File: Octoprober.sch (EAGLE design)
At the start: 101 parts, among them J1 10118193-0001LF, J2 26-60-4020, P1 TC33X-1, SW1 EVQ-Q2203W, SW2 EVQ-Q2203W, SW3 EVQ-Q2203W, SW4 EVQ-Q2203W, SW5 EVQ-Q2203W, U1 P8X32A-M44, U10 MAX31855KASA+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

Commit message: Finished preliminary routing
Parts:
- removed U18: AD7999YRJZ-1500RL7, PP_DigitalIC:AD799XSOT-23-8
- added TC1, TC2, TC3, TC4, TC5, TC6, TC7, TC8: (no value), PP_Connectors:PH_1X02HEADER_PTH
- SW1: value EVQ-Q2203W -> 101-0134-EV; device PP_Electromechanical:SPSTEVQ-Q2203W -> PP_Electromechanical:SPST101-0134-EV
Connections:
- net TP_T+_0: now also TC1.2
- net TP_T+_1: now also TC2.2
- net TP_T+_2: now also TC3.2
- net TP_T+_3: now also TC4.2
- net TP_T+_4: now also TC5.2
- net TP_T+_5: now also TC6.2
- net TP_T+_6: now also TC7.2
- net TP_T+_7: now also TC8.2
- net TP_T-_0: now also TC1.1
- net TP_T-_1: now also TC2.1
- net TP_T-_2: now also TC3.1
- net TP_T-_3: now also TC4.1
- net TP_T-_4: now also TC5.1
- net TP_T-_5: now also TC6.1
- net TP_T-_6: now also TC7.1
- net TP_T-_7: now also TC8.1
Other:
- moved on the sheet: C15, C16, C17, C18, C19, C20, C21, C22, U10, U7, U8, U9

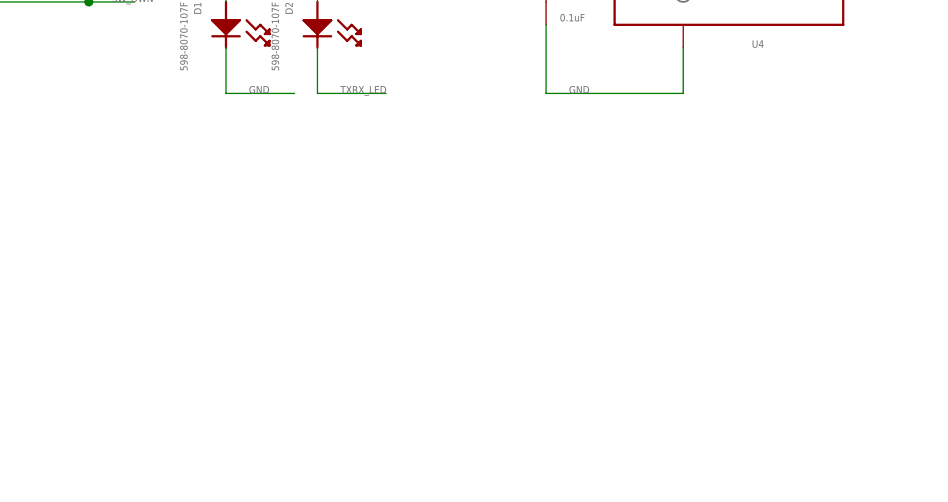
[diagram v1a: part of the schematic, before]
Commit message: Added RTC.
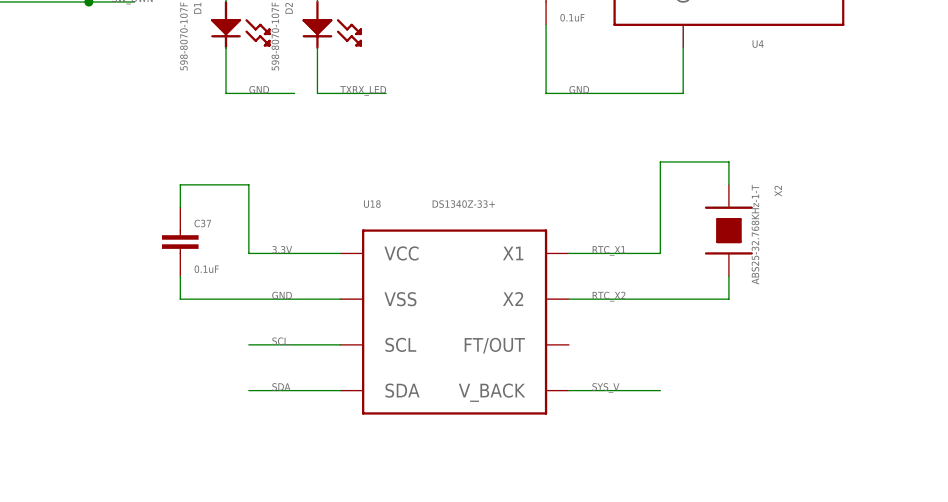
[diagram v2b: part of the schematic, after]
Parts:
- added C37: 0.1uF, PP_Passives:CAPACITOR_NON_POLAR0402
- added U18: DS1340Z-33+, PP_DigitalIC:DS1340SOIC-8
- added X2: ABS25-32.768KHz-1-T, PP_FreqCtrl:CRYSTAL8MM_X_3.8MM
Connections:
- new net RTC_X1: U18.X1, X2.P$1
- new net RTC_X2: U18.X2, X2.P$2
- net 3.3V: now also C37.1, U18.VCC
- net GND: now also C37.2, U18.VSS
- net SCL: now also U18.SCL
- net SDA: now also U18.SDA
- net SYS_V: now also U18.V_BACK
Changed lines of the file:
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@@
 <?xml version="1.0" encoding="utf-8"?>
 <!DOCTYPE eagle SYSTEM "eagle.dtd">
-<eagle version="6.3">
+<eagle version="6.5.0">
 <drawing>
 <settings>
@@
 <grid distance="0.1" unitdist="inch" unit="inch" style="lines" multiple="1" display="no" altdistance="0.01" altunitdist="inch" altunit="inch"/>
 <layers>
-<layer number="1" name="Top" color="14" fill="1" visible="yes" active="no"/>
+<layer number="1" name="Top" color="14" fill="1" visible="no" active="no"/>
 <layer number="2" name="Route2" color="1" fill="3" visible="no" active="no"/>
 <layer number="3" name="Route3" color="4" fill="3" visible="no" active="no"/>
@@
 <layer number="14" name="Route14" color="1" fill="6" visible="no" active="no"/>
 <layer number="15" name="Route15" color="4" fill="6" visible="no" active="no"/>
-<layer number="16" name="Bottom" color="13" fill="1" visible="yes" active="no"/>
-<layer number="17" name="Pads" color="2" fill="1" visible="yes" active="no"/>
-<layer number="18" name="Vias" color="2" fill="1" visible="yes" active="no"/>
-<layer number="19" name="Unrouted" color="6" fill="1" visible="yes" active="no"/>
-<layer number="20" name="Dimension" color="15" fill="1" visible="yes" active="no"/>
-<layer number="21" name="tPlace" color="7" fill="1" visible="yes" active="no"/>
-<layer number="22" name="bPlace" color="7" fill="1" visible="yes" active="no"/>
-<layer number="23" name="tOrigins" color="15" fill="1" visible="yes" active="no"/>
-<layer number="24" name="bOrigins" color="15" fill="1" visible="yes" active="no"/>
-<layer number="25" name="tNames" color="7" fill="1" visible="yes" active="no"/>
-<layer number="26" name="bNames" color="7" fill="1" visible="yes" active="no"/>
-<layer number="27" name="tValues" color="7" fill="1" visible="yes" active="no"/>
-<layer number="28" name="bValues" color="7" fill="1" visible="yes" active="no"/>
+<layer number="16" name="Bottom" color="13" fill="1" visible="no" active="no"/>
+<layer number="17" name="Pads" color="2" fill="1" visible="no" active="no"/>
+<layer number="18" name="Vias" color="2" fill="1" visible="no" active="no"/>
+<layer number="19" name="Unrouted" color="6" fill="1" visible="no" active="no"/>
+<layer number="20" name="Dimension" color="15" fill="1" visible="no" active="no"/>
+<layer number="21" name="tPlace" color="7" fill="1" visible="no" active="no"/>
+<layer number="22" name="bPlace" color="7" fill="1" visible="no" active="no"/>
+<layer number="23" name="tOrigins" color="15" fill="1" visible="no" active="no"/>
+<layer number="24" name="bOrigins" color="15" fill="1" visible="no" active="no"/>
+<layer number="25" name="tNames" color="7" fill="1" visible="no" active="no"/>
+<layer number="26" name="bNames" color="7" fill="1" visible="no" active="no"/>
+<layer number="27" name="tValues" color="7" fill="1" visible="no" active="no"/>
+<layer number="28" name="bValues" color="7" fill="1" visible="no" active="no"/>
 <layer number="29" name="tStop" color="7" fill="3" visible="no" active="no"/>
 <layer number="30" name="bStop" color="7" fill="6" visible="no" active="no"/>
@@
 <layer number="35" name="tGlue" color="7" fill="4" visible="no" active="no"/>
 <layer number="36" name="bGlue" color="7" fill="5" visible="no" active="no"/>
-<layer number="37" name="tTest" color="7" fill="1" visible="yes" active="no"/>
-<layer number="38" name="bTest" color="7" fill="1" visible="yes" active="no"/>
+<layer number="37" name="tTest" color="7" fill="1" visible="no" active="no"/>
+<layer number="38" name="bTest" color="7" fill="1" visible="no" active="no"/>
 <layer number="39" name="tKeepout" color="4" fill="11" visible="no" active="no"/>
 <layer number="40" name="bKeepout" color="1" fill="11" visible="no" active="no"/>
@@
 <layer number="44" name="Drills" color="7" fill="1" visible="no" active="no"/>
 <layer number="45" name="Holes" color="7" fill="1" visible="no" active="no"/>
-<layer number="46" name="Milling" color="3" fill="1" visible="yes" active="no"/>
-<layer number="47" name="Measures" color="7" fill="1" visible="yes" active="no"/>
-<layer number="48" name="Document" color="7" fill="1" visible="yes" active="no"/>
-<layer number="49" name="Reference" color="7" fill="1" visible="yes" active="no"/>
-<layer number="50" name="dxf" color="7" fill="1" visible="yes" active="no"/>
-<layer number="51" name="tDocu" color="7" fill="1" visible="yes" active="no"/>
-<layer number="52" name="bDocu" color="7" fill="1" visible="yes" active="no"/>
-<layer number="53" name="tGND_GNDA" color="7" fill="9" visible="yes" active="no"/>
-<layer number="54" name="bGND_GNDA" color="1" fill="9" visible="yes" active="no"/>
-<layer number="56" name="wert" color="7" fill="1" visible="yes" active="no"/>
+<layer number="46" name="Milling" color="3" fill="1" visible="no" active="no"/>
+<layer number="47" name="Measures" color="7" fill="1" visible="no" active="no"/>
+<layer number="48" name="Document" color="7" fill="1" visible="no" active="no"/>
+<layer number="49" name="Reference" color="7" fill="1" visible="no" active="no"/>
+<layer number="50" name="dxf" color="7" fill="1" visible="no" active="no"/>
+<layer number="51" name="tDocu" color="7" fill="1" visible="no" active="no"/>
+<layer number="52" name="bDocu" color="7" fill="1" visible="no" active="no"/>
+<layer number="53" name="tGND_GNDA" color="7" fill="9" visible="no" active="no"/>
+<layer number="54" name="bGND_GNDA" color="1" fill="9" visible="no" active="no"/>
+<layer number="56" name="wert" color="7" fill="1" visible="no" active="no"/>
 <layer number="91" name="Nets" color="2" fill="1" visible="yes" active="yes"/>
 <layer number="92" name="Busses" color="1" fill="1" visible="yes" active="yes"/>
@@
 <part name="TC7" library="PP_Connectors" deviceset="PH_1X02" device="HEADER_PTH"/>
 <part name="TC8" library="PP_Connectors" deviceset="PH_1X02" device="HEADER_PTH"/>
+<part name="U18" library="PP_DigitalIC" deviceset="DS1340" device="SOIC-8" value="DS1340Z-33+"/>
+<part name="C37" library="PP_Passives" deviceset="CAPACITOR_NON_POLAR" device="0402" value="0.1uF"/>
+<part name="X2" library="PP_FreqCtrl" deviceset="CRYSTAL" device="8MM_X_3.8MM" value="ABS25-32.768KHz-1-T"/>
 </parts>
 <sheets>
@@
 <instance part="TC7" gate="G$1" x="-233.68" y="-43.18" rot="R180"/>
 <instance part="TC8" gate="G$1" x="-233.68" y="-68.58" rot="R180"/>
+<instance part="U18" gate="G$1" x="-91.44" y="-111.76"/>
+<instance part="C37" gate="G$1" x="-121.92" y="-101.6"/>
+<instance part="X2" gate="G$1" x="-60.96" y="-101.6" rot="R270"/>
 </instances>
 <busses>
@@
 <label x="55.88" y="7.62" size="0.8128" layer="95" font="vector"/>
 </segment>
+<segment>
+<pinref part="U18" gate="G$1" pin="SDA"/>
+<wire x1="-104.14" y1="-119.38" x2="-114.3" y2="-119.38" width="0.1524" layer="91"/>
+<label x="-111.76" y="-119.38" size="0.8128" layer="95" font="vector"/>
+</segment>
 </net>
 <net name="SCL" class="0">
@@
 <wire x1="53.34" y1="12.7" x2="60.96" y2="12.7" width="0.1524" layer="91"/>
 <label x="55.88" y="12.7" size="0.8128" layer="95" font="vector"/>
+</segment>
+<segment>
+<pinref part="U18" gate="G$1" pin="SCL"/>
+<wire x1="-104.14" y1="-114.3" x2="-114.3" y2="-114.3" width="0.1524" layer="91"/>
+<label x="-111.76" y="-114.3" size="0.8128" layer="95" font="vector"/>
 </segment>
 </net>
@@
 <wire x1="12.7" y1="-101.6" x2="7.62" y2="-101.6" width="0.1524" layer="91"/>
 <label x="7.62" y="-101.6" size="0.8128" layer="95" font="vector"/>
+</segment>
+<segment>
+<pinref part="U18" gate="G$1" pin="VSS"/>
+<wire x1="-104.14" y1="-109.22" x2="-121.92" y2="-109.22" width="0.1524" layer="91"/>
+<label x="-111.76" y="-109.22" size="0.8128" layer="95" font="vector"/>
+<pinref part="C37" gate="G$1" pin="2"/>
+<wire x1="-121.92" y1="-109.22" x2="-121.92" y2="-106.68" width="0.1524" layer="91"/>
 </segment>
 </net>
@@
 <junction x="139.7" y="-55.88"/>
 </segment>
+<segment>
+<pinref part="U18" gate="G$1" pin="VCC"/>
+<wire x1="-104.14" y1="-104.14" x2="-114.3" y2="-104.14" width="0.1524" layer="91"/>
+<label x="-111.76" y="-104.14" size="0.8128" layer="95" font="vector"/>
+<wire x1="-114.3" y1="-104.14" x2="-114.3" y2="-96.52" width="0.1524" layer="91"/>
+<wire x1="-114.3" y1="-96.52" x2="-121.92" y2="-96.52" width="0.1524" layer="91"/>
+<pinref part="C37" gate="G$1" pin="1"/>
+<wire x1="-121.92" y1="-96.52" x2="-121.92" y2="-99.06" width="0.1524" layer="91"/>
+</segment>
 </net>
 <net name="SD_RW" class="0">
@@
 <junction x="78.74" y="-50.8"/>
 </segment>
+<segment>
+<pinref part="U18" gate="G$1" pin="V_BACK"/>
+<wire x1="-68.58" y1="-119.38" x2="-78.74" y2="-119.38" width="0.1524" layer="91"/>
+<label x="-76.2" y="-119.38" size="0.8128" layer="95" font="vector"/>
+</segment>
 </net>
 <net name="BCD_CHARGER" class="0">
@@
 </segment>
 </net>
+<net name="RTC_X1" class="0">
+<segment>
+<pinref part="U18" gate="G$1" pin="X1"/>
+<wire x1="-78.74" y1="-104.14" x2="-68.58" y2="-104.14" width="0.1524" layer="91"/>
+<label x="-76.2" y="-104.14" size="0.8128" layer="95" font="vector"/>
+<wire x1="-68.58" y1="-104.14" x2="-68.58" y2="-93.98" width="0.1524" layer="91"/>
+<wire x1="-68.58" y1="-93.98" x2="-60.96" y2="-93.98" width="0.1524" layer="91"/>
+<pinref part="X2" gate="G$1" pin="P$1"/>
+<wire x1="-60.96" y1="-93.98" x2="-60.96" y2="-96.52" width="0.1524" layer="91"/>
+</segment>
+</net>
+<net name="RTC_X2" class="0">
+<segment>
+<pinref part="U18" gate="G$1" pin="X2"/>
+<wire x1="-60.96" y1="-109.22" x2="-78.74" y2="-109.22" width="0.1524" layer="91"/>
+<label x="-76.2" y="-109.22" size="0.8128" layer="95" font="vector"/>
+<pinref part="X2" gate="G$1" pin="P$2"/>
+<wire x1="-60.96" y1="-106.68" x2="-60.96" y2="-109.22" width="0.1524" layer="91"/>
+</segment>
+</net>

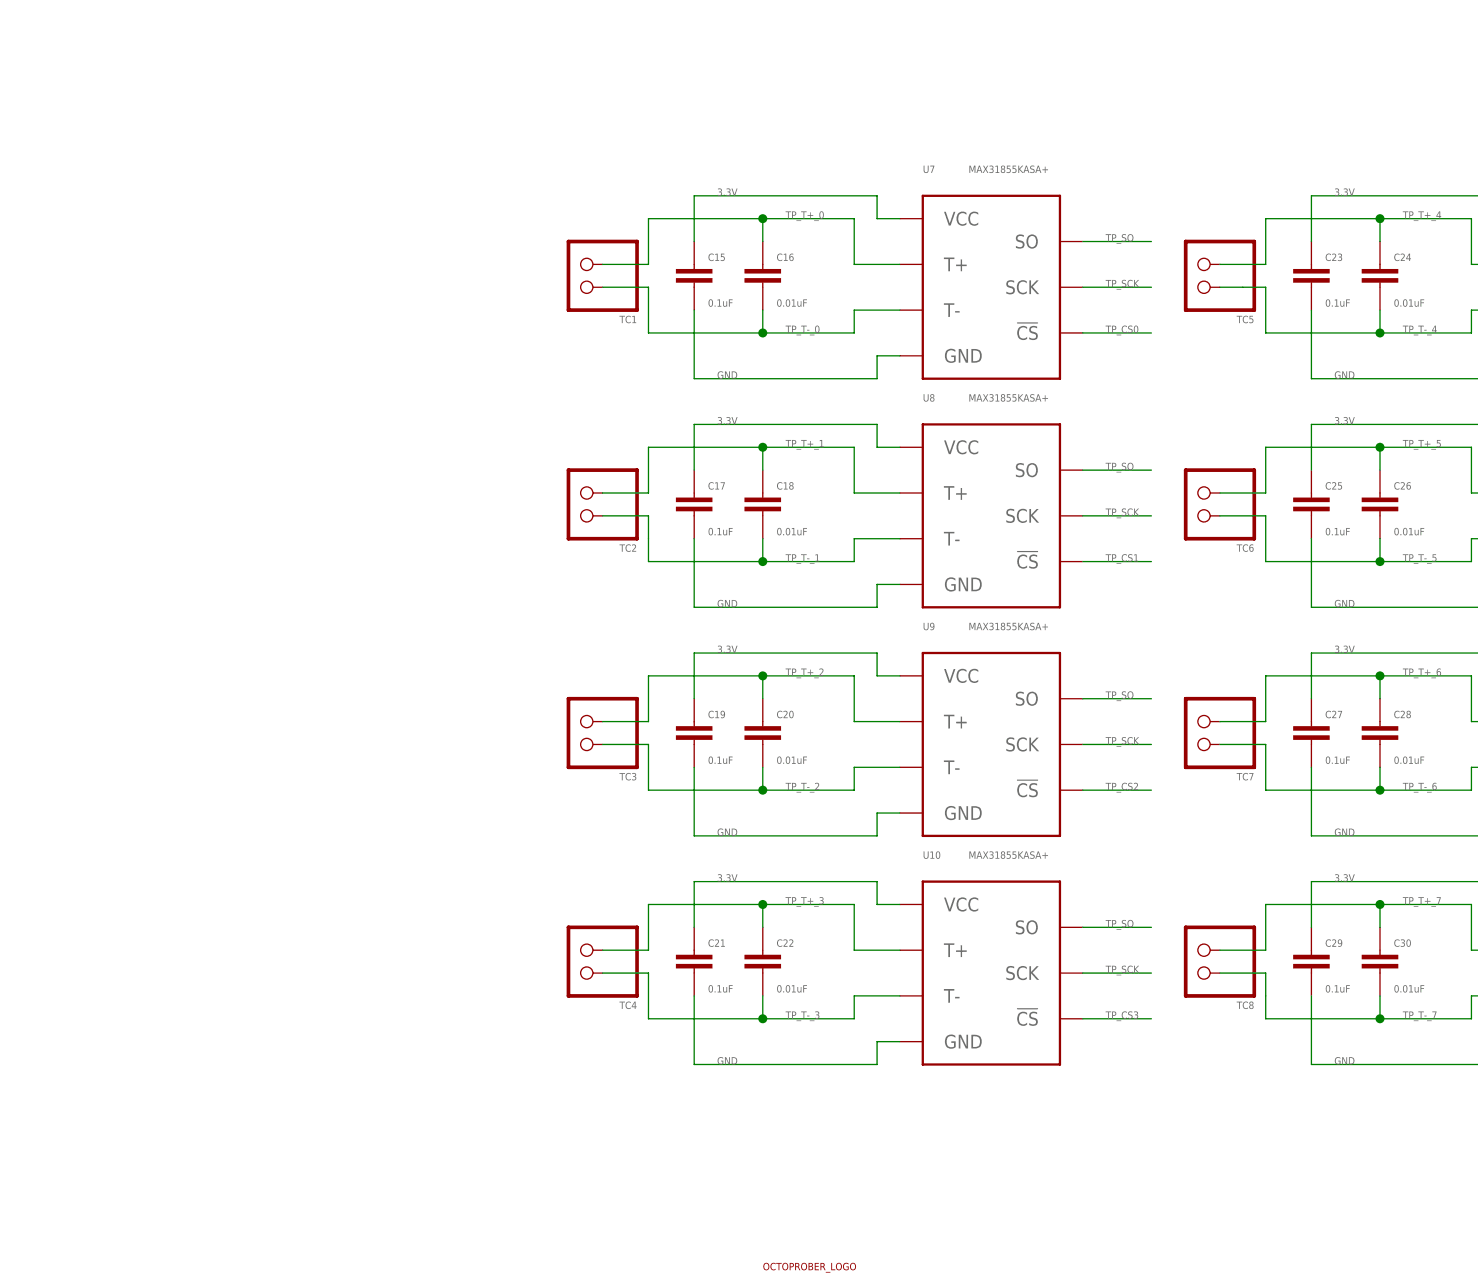
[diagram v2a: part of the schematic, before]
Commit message: Added TVS to TC lines.
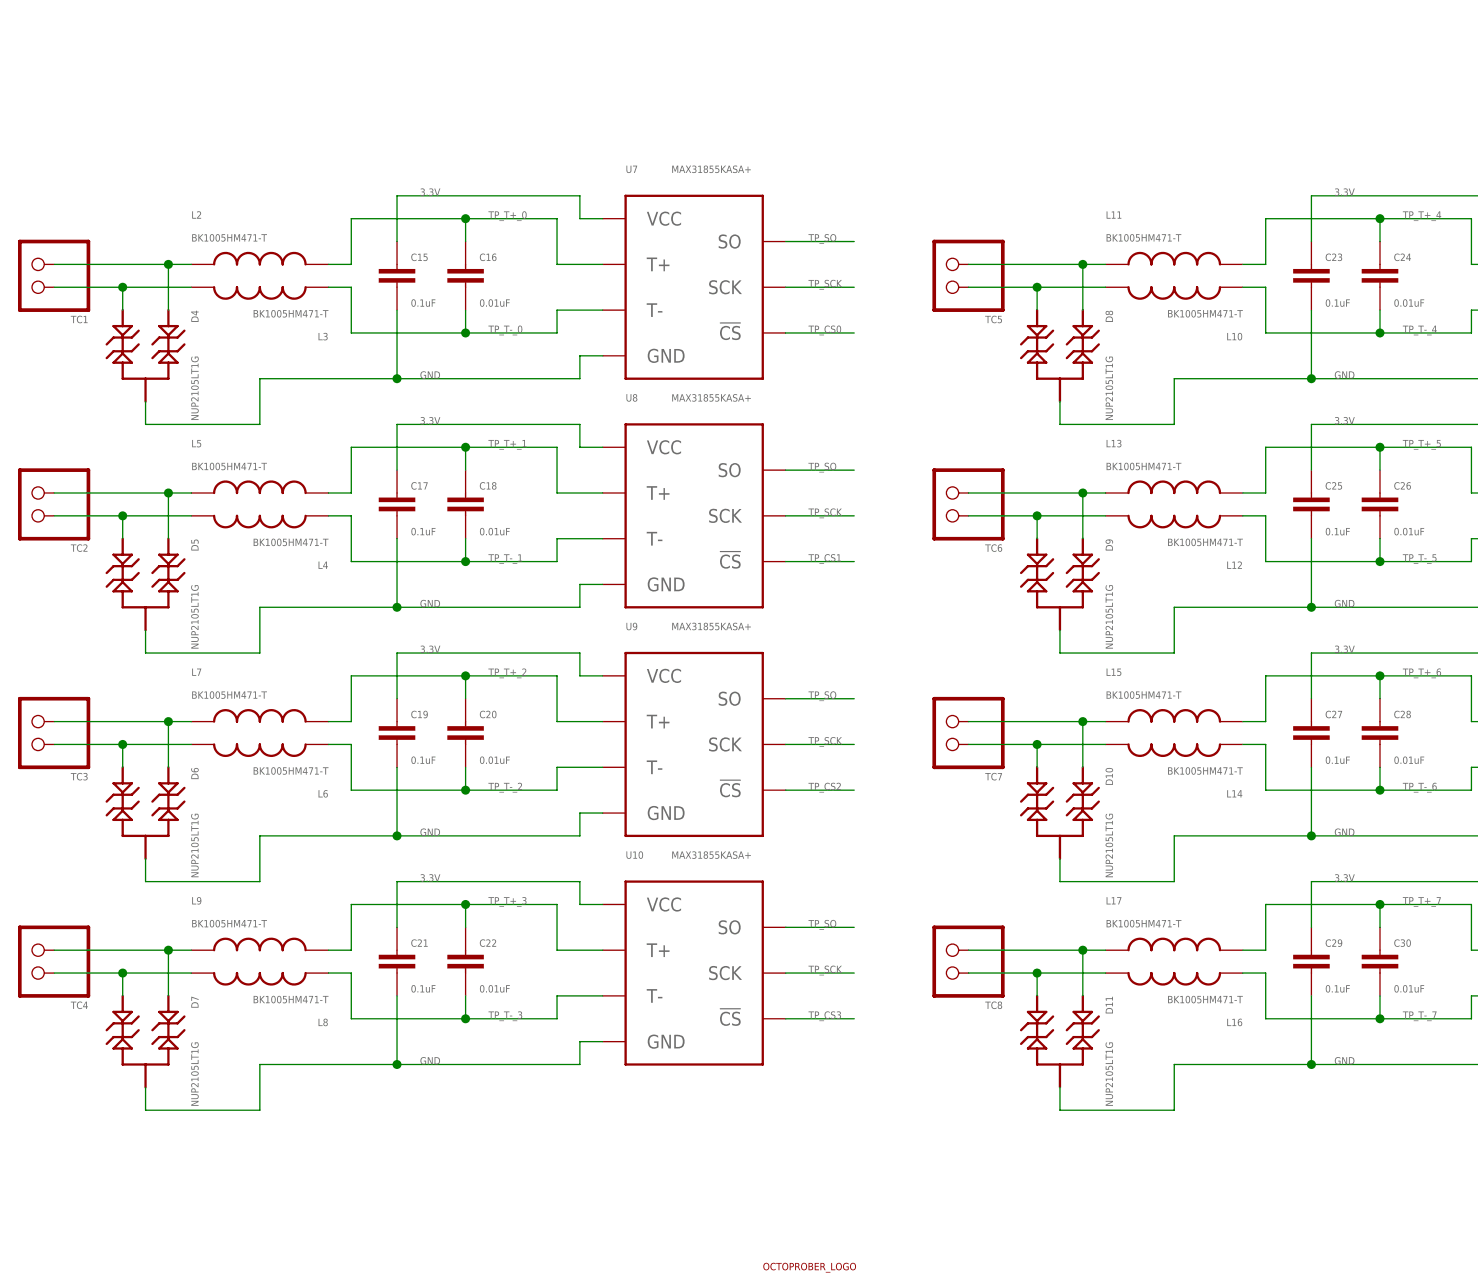
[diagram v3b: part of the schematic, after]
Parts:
- added D10, D11, D4, D5, D6, D7, D8, D9: NUP2105LT1G, PP_Passives:TVS_DIODE_DUALSOT-23
- added L10, L11, L12, L13, L14, L15, L16, L17, L2, L3, L4, L5, L6, L7, L8, L9: BK1005HM471-T, PP_Passives:INDUCTOR0402
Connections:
- new net N$10: D6.1, L7.P$1, TC3.2
- new net N$11: D6.2, L6.P$2, TC3.1
- new net N$12: D7.1, L9.P$1, TC4.2
- new net N$13: D7.2, L8.P$2, TC4.1
- new net N$14: D11.1, L17.P$1, TC8.2
- new net N$15: D11.2, L16.P$2, TC8.1
- new net N$16: D10.1, L15.P$1, TC7.2
- new net N$17: D10.2, L14.P$2, TC7.1
- new net N$18: D9.1, L13.P$1, TC6.2
- new net N$19: D9.2, L12.P$2, TC6.1
- new net N$2: D4.1, L2.P$1, TC1.2
- new net N$20: D8.1, L11.P$1, TC5.2
- new net N$21: D8.2, L10.P$2, TC5.1
- new net N$7: D4.2, L3.P$2, TC1.1
- new net N$8: D5.1, L5.P$1, TC2.2
- new net N$9: D5.2, L4.P$2, TC2.1
- net GND: now also D10.3, D11.3, D4.3, D5.3, D6.3, D7.3, D8.3, D9.3
- net TP_T+_0: now also L2.P$2; no longer TC1.2
- net TP_T+_1: now also L5.P$2; no longer TC2.2
- net TP_T+_2: now also L7.P$2; no longer TC3.2
- net TP_T+_3: now also L9.P$2; no longer TC4.2
- net TP_T+_4: now also L11.P$2; no longer TC5.2
- net TP_T+_5: now also L13.P$2; no longer TC6.2
- net TP_T+_6: now also L15.P$2; no longer TC7.2
- net TP_T+_7: now also L17.P$2; no longer TC8.2
- net TP_T-_0: now also L3.P$1; no longer TC1.1
- net TP_T-_1: now also L4.P$1; no longer TC2.1
- net TP_T-_2: now also L6.P$1; no longer TC3.1
- net TP_T-_3: now also L8.P$1; no longer TC4.1
- net TP_T-_4: now also L10.P$1; no longer TC5.1
- net TP_T-_5: now also L12.P$1; no longer TC6.1
- net TP_T-_6: now also L14.P$1; no longer TC7.1
- net TP_T-_7: now also L16.P$1; no longer TC8.1
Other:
- moved on the sheet: C15, C16, C17, C18, C19, C20, C21, C22, TC1, TC2, TC3, TC4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
